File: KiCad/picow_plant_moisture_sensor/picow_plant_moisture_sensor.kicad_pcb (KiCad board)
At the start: 2 copper layers, 80 x 72.4 mm, 61 parts, among them J1 Conn_01x03, J10 Conn_01x03, J11 Conn_01x03, J12 Conn_01x03, J13 Conn_02x03_Odd_Even, J14 Conn_01x03, J15 Conn_01x03, J16 Conn_01x03, J17 Conn_01x03, J2 Conn_01x03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

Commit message: Routing done
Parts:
- removed TP3, TP4: TestPoint, TestPoint:TestPoint_Pad_D2.0mm
- moved SW4 50.9 mm to (109.6, 52.1)
- moved SW2 47.6 mm to (102.0, 48.3)
- moved SW3 40.0 mm to (102.0, 56.6)
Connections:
- J14 pad 3: unconnected-(J14-Pin_3-Pad3) -> /AIN12
- R18 pad 2: /GPIO22 -> /GPIO2
- R19 pad 2: /GPIO21 -> /GPIO3
- R20 pad 2: /GPIO20 -> /GPIO4
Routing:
- net /AIN15: track 0.00 -> 82.6 mm, vias 0 -> 1
- net /AIN14: track 0.00 -> 82.2 mm, vias 0 -> 1
- net /AIN11: track 0.00 -> 75.6 mm, vias 0 -> 3
- net /AIN12: track 0.00 -> 65.5 mm
- net /AIN13: track 0.00 -> 62.3 mm
- net /AIN0: track 0.00 -> 60.0 mm, vias 0 -> 1
- net /GPIO9: track 0.00 -> 53.4 mm, vias 0 -> 4
- net /AIN1: track 0.00 -> 53.1 mm, vias 0 -> 1
- net /GPIO8: track 0.00 -> 46.0 mm
- net Net-(R15-Pad2): track 0.00 -> 44.9 mm, vias 0 -> 2
- net /AIN2: track 0.00 -> 44.6 mm, vias 0 -> 1
- net +3V3: track 0.00 -> 36.9 mm, vias 0 -> 10
- net /AIN4: track 0.00 -> 36.6 mm, vias 0 -> 1
- net /GPIO4: track 0.00 -> 35.0 mm, vias 0 -> 2
- net /GPIO3: track 0.00 -> 34.6 mm, vias 0 -> 2
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- added copper zone on In1.Cu, net +3V3
- added copper zone on In2.Cu, net GND
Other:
- copper layers 2 -> 4
- board text removed: "SCL"
- board text removed: "SDA"

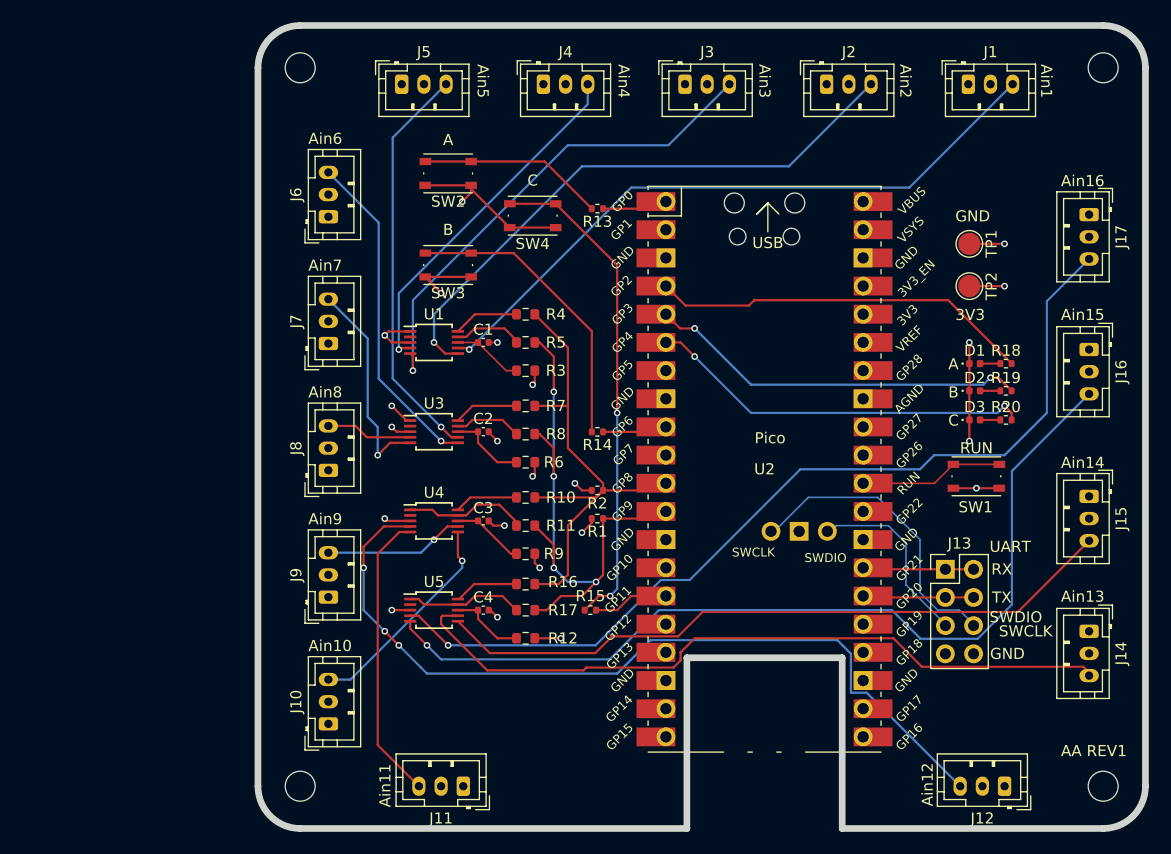
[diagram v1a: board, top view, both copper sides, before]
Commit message: Complete PCB design with component references
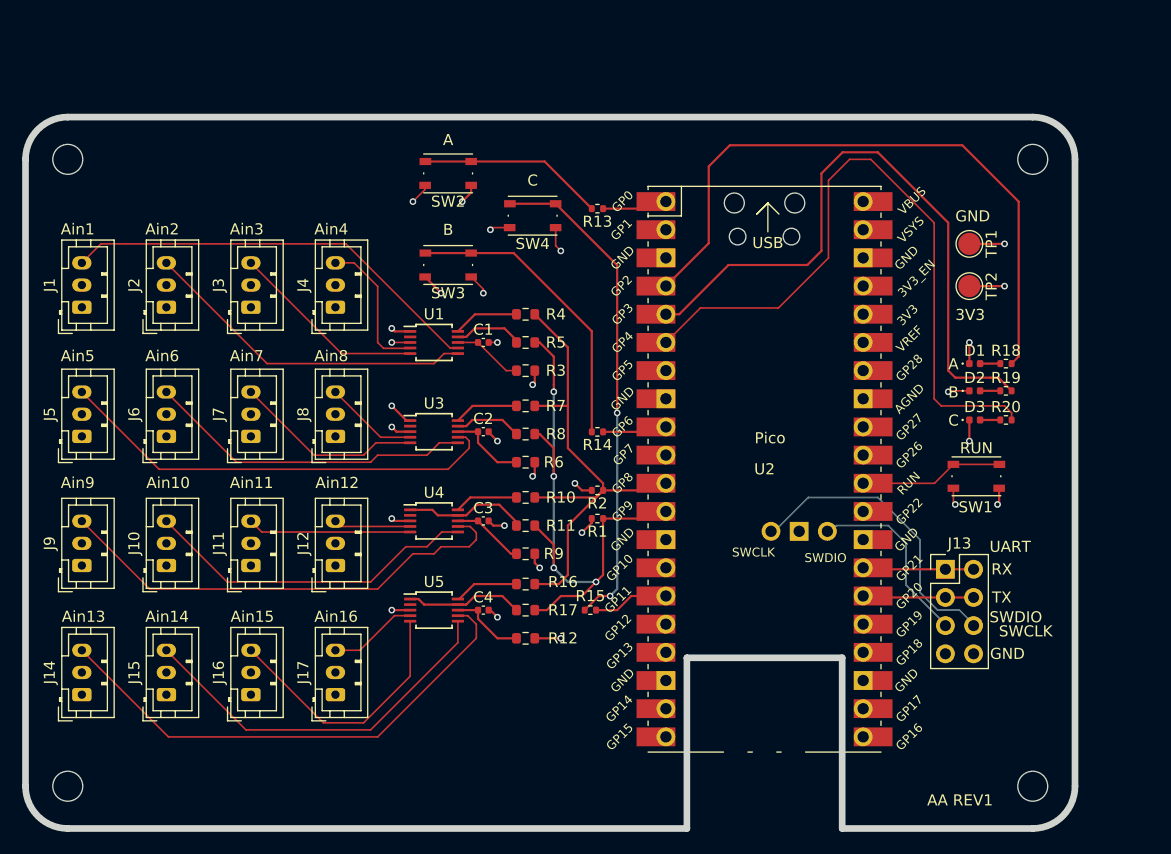
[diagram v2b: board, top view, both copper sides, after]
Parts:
- moved J14 91.0 mm to (69.0, 95.3), turned to 90 degrees
- moved J15 85.1 mm to (76.6, 95.3), turned to 90 degrees
- moved J1 82.4 mm to (69.0, 60.4), turned to 90 degrees
- moved J16 81.7 mm to (84.2, 95.3), turned to 90 degrees
- moved J17 80.6 mm to (91.8, 95.3), turned to 90 degrees
- moved J12 63.5 mm to (91.8, 83.7), turned to 90 degrees
- moved J2 62.8 mm to (76.6, 60.4), turned to 90 degrees
- moved J3 44.0 mm to (84.2, 60.4), turned to 90 degrees
- moved J5 42.9 mm to (69.0, 72.0), turned to 90 degrees
- moved J11 27.6 mm to (84.2, 83.7), turned to 90 degrees
- moved J4 27.5 mm to (91.8, 60.4), turned to 90 degrees
- moved J6 24.6 mm to (76.6, 72.0)
- moved H2 22.5 mm to (67.7, 47.1)
- moved J9 22.4 mm to (69.0, 83.7)
- moved H4 21.0 mm to (67.7, 103.6)
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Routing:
- net /AIN15: track 82.6 -> 8.03 mm, vias 1 -> 0
- net /AIN11: track 75.6 -> 6.94 mm, vias 3 -> 0
- net /AIN14: track 82.2 -> 23.8 mm, vias 1 -> 0
- net /AIN8: track 12.7 -> 42.5 mm, vias 1 -> 0
- net /AIN13: track 62.3 -> 34.4 mm
- net /AIN2: track 44.6 -> 17.7 mm, vias 1 -> 0
- net /GPIO4: track 35.0 -> 61.5 mm, vias 2 -> 0
- net /GPIO2: track 34.5 -> 58.1 mm
- net /GPIO3: track 34.6 -> 58.0 mm, vias 2 -> 0
- net /AIN1: track 53.1 -> 30.4 mm, vias 1 -> 0
- net /AIN0: track 60.0 -> 38.5 mm, vias 1 -> 0
- net /AIN12: track 65.5 -> 45.7 mm
- net /AIN3: track 32.1 -> 12.9 mm, vias 1 -> 0
- net /AIN10: track 26.2 -> 14.8 mm
- net /AIN9: track 19.6 -> 30.4 mm, vias 1 -> 0
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- added copper zone on In2.Cu, net +3V3
- added copper zone on In1.Cu, net GND
- removed copper zone on In1.Cu, net +3V3
- removed copper zone on In2.Cu, net GND
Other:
- board size 80 x 72.4 mm -> 94.6 x 64.1 mm
